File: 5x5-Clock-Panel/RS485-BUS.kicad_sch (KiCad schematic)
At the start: 1 part

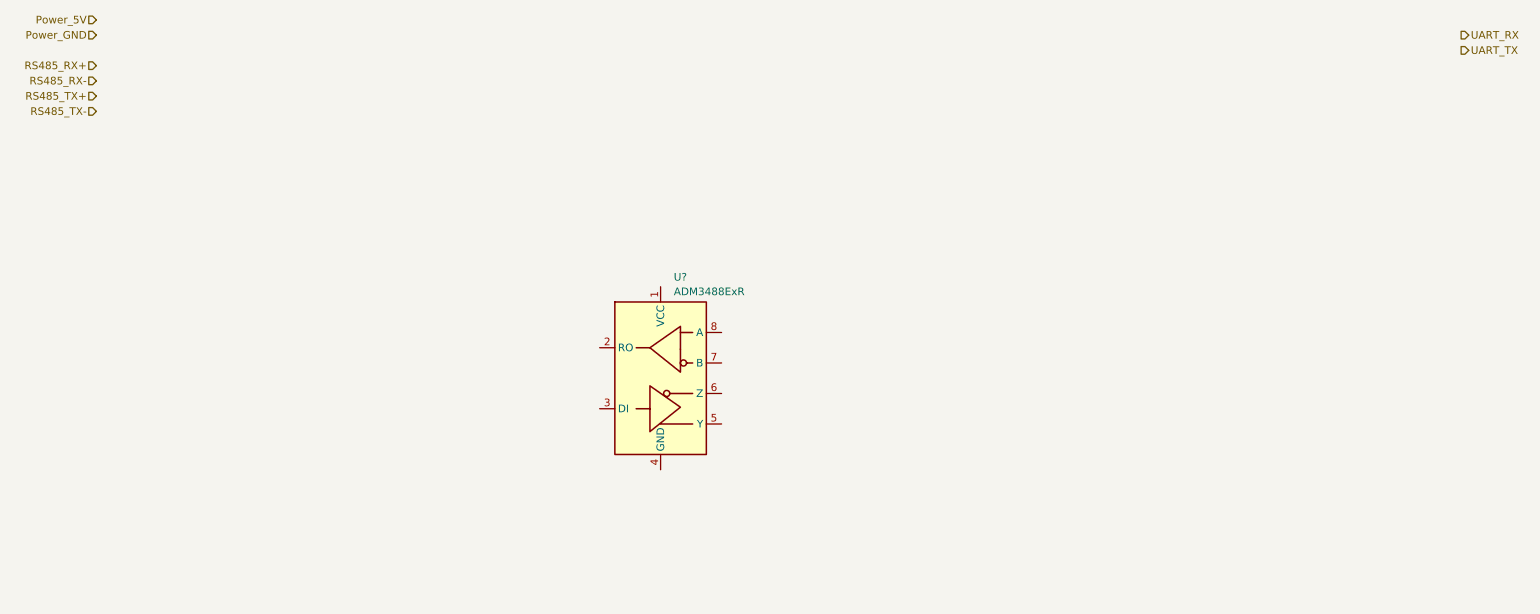
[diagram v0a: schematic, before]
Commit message: added rs485 tranceiver
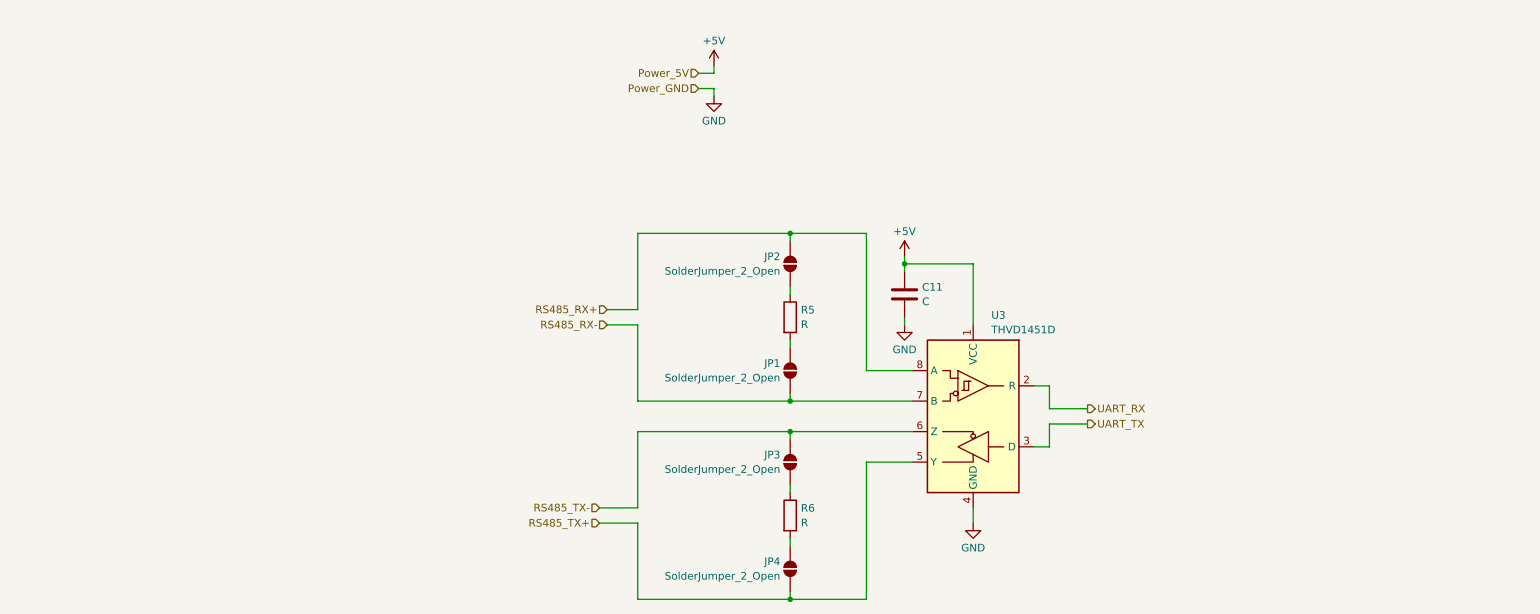
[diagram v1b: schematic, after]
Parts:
- removed U?: ADM3488ExR, Package_SO:SOIC-8_3.9x4.9mm_P1.27mm, symbol Interface_UART:ADM3488ExR
- added C11: C, symbol Device:C
- added JP1, JP2, JP3, JP4: SolderJumper_2_Open, symbol Jumper:SolderJumper_2_Open
- added R5, R6: R, symbol Device:R
- added U3: THVD1451D, Package_SO:SOIC-8_3.9x4.9mm_P1.27mm, symbol Interface_UART:THVD1451D
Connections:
- net RS485_RX+: now also JP2.2 (B), U3.8 (A)
- net RS485_RX-: now also JP1.1 (A), U3.7 (B)
- net RS485_TX+: now also JP4.1 (A), U3.5 (Y)
- net RS485_TX-: now also JP3.2 (B), U3.6 (Z)
- net UART_RX: now also U3.2 (R)
- net UART_TX: now also U3.3 (D)
- new net: JP1.2 (B), R5.2
- new net: JP2.1 (A), R5.1
- new net: JP3.1 (A), R6.1
- new net: JP4.2 (B), R6.2
- new net +5V: C11.1, U3.1 (VCC)
- new net GND: C11.2, U3.4 (GND)
